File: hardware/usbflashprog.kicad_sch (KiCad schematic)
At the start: 13 parts, among them J1 12-18V, J2 Parallel Adapter, J3 Serial Adapter, U1 7809

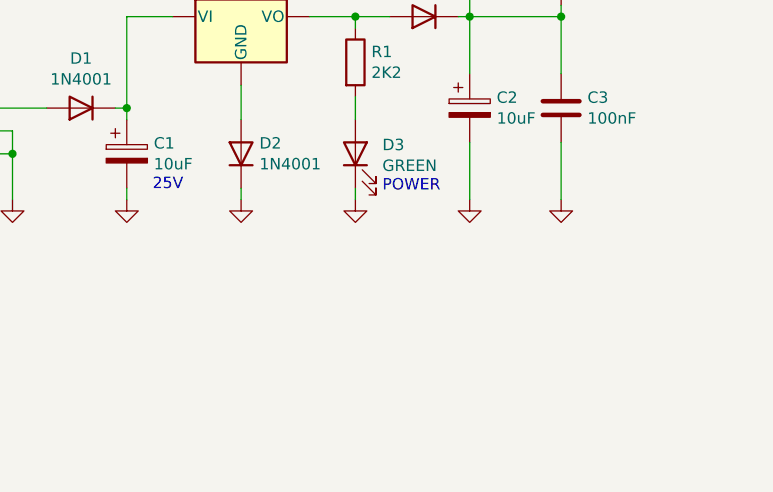
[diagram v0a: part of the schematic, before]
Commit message: Rev.E. Updated hardware design.
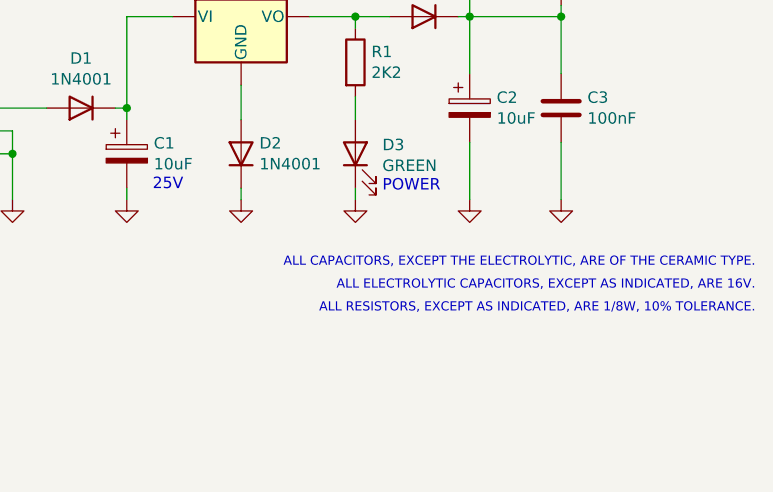
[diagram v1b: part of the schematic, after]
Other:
- note added: "ALL CAPACITORS, EXCEPT THE ELECTROLYTIC, ARE OF THE CERAMIC TYPE."
- note added: "ALL ELECTROLYTIC CAPACITORS, EXCEPT AS INDICATED, ARE 16V."
- note added: "ALL RESISTORS, EXCEPT AS INDICATED, ARE 1/8W, 10% TOLERANCE."
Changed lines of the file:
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@@
   (title_block
     (title "USB Flash/EPROM Programmer")
-    (date "2022-04-23")
+    (date "2022-04-27")
     (rev "v0.1.0 rev.E")
     (company "Robson Martins")
@@
     (effects (font (size 1.27 1.27)) (justify left bottom))
   )
+  (text "ALL CAPACITORS, EXCEPT THE ELECTROLYTIC, ARE OF THE CERAMIC TYPE."
+    (at 283.21 160.02 0)
+    (effects (font (size 1.016 1.016)) (justify right bottom))
+  )
   (text "VDD" (at 228.6 53.34 180)
     (effects (font (size 1.27 1.27)) (justify right bottom))
   )
+  (text "ALL RESISTORS, EXCEPT AS INDICATED, ARE 1/8W, 10% TOLERANCE."
+    (at 283.21 165.1 0)
+    (effects (font (size 1.016 1.016)) (justify right bottom))
+  )
   (text "*NC" (at 152.4 50.8 0)
     (effects (font (size 1.27 1.27)) (justify left bottom))
@@
     (effects (font (size 1.27 1.27)) (justify right bottom))
   )
+  (text "ALL ELECTROLYTIC CAPACITORS, EXCEPT AS INDICATED, ARE 16V."
+    (at 283.21 162.56 0)
+    (effects (font (size 1.016 1.016)) (justify right bottom))
+  )
   (label "D7" (at 152.4 81.28 0)

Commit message: Rev.E. Updated specifications document and hardware design.
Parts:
- C1, C2: footprint Capacitor_THT:CP_Radial_D8.0mm_P3.50mm -> (none)
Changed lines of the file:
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@@
       (effects (font (size 1.27 1.27)) (justify left))
     )
-    (property "Footprint" "Capacitor_THT:CP_Radial_D8.0mm_P3.50mm" (id 2) (at 214.3252 151.13 0)
+    (property "Footprint" "" (id 2) (at 214.3252 151.13 0)
       (effects (font (size 1.27 1.27)) hide)
     )
@@
       (effects (font (size 1.27 1.27)) (justify left))
     )
-    (property "Footprint" "Capacitor_THT:CP_Radial_D8.0mm_P3.50mm" (id 2) (at 252.4252 146.05 0)
+    (property "Footprint" "" (id 2) (at 252.4252 146.05 0)
       (effects (font (size 1.27 1.27)) hide)
     )
@@
     )
     (path "/00000000-0000-0000-0000-0000626538df"
-      (reference "C1") (unit 1) (value "10uF") (footprint "Capacitor_THT:CP_Radial_D8.0mm_P3.50mm")
+      (reference "C1") (unit 1) (value "10uF") (footprint "Capacitor_THT:CP_Radial_D5.0mm_P2.50mm")
     )
     (path "/00000000-0000-0000-0000-0000626542c9"
-      (reference "C2") (unit 1) (value "10uF") (footprint "Capacitor_THT:CP_Radial_D8.0mm_P3.50mm")
+      (reference "C2") (unit 1) (value "10uF") (footprint "Capacitor_THT:CP_Radial_D5.0mm_P2.50mm")
     )
     (path "/00000000-0000-0000-0000-00006265f2db"
@@
     )
     (path "/00000000-0000-0000-0000-0000626cc8f1/00000000-0000-0000-0000-0000626ea7f4"
-      (reference "C4") (unit 1) (value "470uF") (footprint "Capacitor_THT:CP_Radial_D10.0mm_P7.50mm")
+      (reference "C4") (unit 1) (value "470uF") (footprint "Capacitor_THT:CP_Radial_D8.0mm_P3.80mm")
     )
     (path "/00000000-0000-0000-0000-0000626cc8f1/00000000-0000-0000-0000-0000626ea7fa"
@@
     )
     (path "/00000000-0000-0000-0000-0000626cc8f1/00000000-0000-0000-0000-0000627c025d"
-      (reference "C6") (unit 1) (value "22uF") (footprint "Capacitor_THT:CP_Radial_D8.0mm_P3.50mm")
+      (reference "C6") (unit 1) (value "22uF") (footprint "Capacitor_THT:CP_Radial_D5.0mm_P2.50mm")
     )
     (path "/00000000-0000-0000-0000-00006268ec8d/00000000-0000-0000-0000-000062672922"
@@
     )
     (path "/00000000-0000-0000-0000-00006268ec8d/00000000-0000-0000-0000-000062694864"
-      (reference "C8") (unit 1) (value "100uF") (footprint "Capacitor_THT:C_Disc_D6.0mm_W2.5mm_P5.00mm")
+      (reference "C8") (unit 1) (value "100uF") (footprint "Capacitor_THT:CP_Radial_D8.0mm_P3.50mm")
     )
     (path "/00000000-0000-0000-0000-00006268ec8d/00000000-0000-0000-0000-000062694ee8"
@@
     )
     (path "/00000000-0000-0000-0000-00006268ec8d/00000000-0000-0000-0000-000062697554"
-      (reference "L2") (unit 1) (value "300uH") (footprint "Inductor_THT:L_Toroid_Vertical_L16.0mm_W8.0mm_P7.62mm")
+      (reference "L2") (unit 1) (value "300uH") (footprint "Inductor_THT:L_Toroid_Vertical_L13.0mm_W6.5mm_P5.60mm")
     )
     (path "/00000000-0000-0000-0000-0000626cc8f1/00000000-0000-0000-0000-0000626ef1cc"
@@
     )
     (path "/00000000-0000-0000-0000-0000627eb794/3cd54b60-8f9b-46d2-82ca-584e18d4e3bd"
-      (reference "R52") (unit 1) (value "560R") (footprint "Resistor_THT:R_Axial_DIN0207_L6.3mm_D2.5mm_P10.16mm_Horizontal")
+      (reference "R52") (unit 1) (value "560R") (footprint "Resistor_THT:R_Axial_DIN0309_L9.0mm_D3.2mm_P15.24mm_Horizontal")
     )
     (path "/00000000-0000-0000-0000-000062654db0"

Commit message: Rev.E. Updated R51 wattage.
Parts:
- C1, C2: footprint (none) -> Capacitor_THT:CP_Radial_D5.0mm_P2.50mm
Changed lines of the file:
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@@
       (effects (font (size 1.27 1.27)) (justify left))
     )
-    (property "Footprint" "" (id 2) (at 214.3252 151.13 0)
+    (property "Footprint" "Capacitor_THT:CP_Radial_D5.0mm_P2.50mm" (id 2) (at 214.3252 151.13 0)
       (effects (font (size 1.27 1.27)) hide)
     )
@@
       (effects (font (size 1.27 1.27)) (justify left))
     )
-    (property "Footprint" "" (id 2) (at 252.4252 146.05 0)
+    (property "Footprint" "Capacitor_THT:CP_Radial_D5.0mm_P2.50mm" (id 2) (at 252.4252 146.05 0)
       (effects (font (size 1.27 1.27)) hide)
     )
